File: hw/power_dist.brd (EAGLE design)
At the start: 80 x 50 mm, 78 parts, among them J1 JST-ZH6SMT_VERT, J2 JST-PH4SMT_VERT, J3 JST-PH5VERT, P1 XT30P, P2 XT30P, P3 XT30P, P4 XT30P, P5 XT30P, P6 XT30P, P7 XT90PW-M, Q1 PSMN4R8-100BSEJ, Q2 PSMN4R8-100BSEJ, Q3 PSMN4R8-100BSEJ, Q4 MF-DSC-SOT233-MMBT3904, Q5 MMBT5401 100V, U1 MAX15062AATA+T, U2 STM32G474CEU6, U4 TCAN334G, U5 LT1787HVIMS8PBF, U6 LTC4830, X3 FSV10150VTO277-3L_ONS-L

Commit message: Fine place silks
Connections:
- net GND: no longer D3.2
- net PGND: now also D3.2
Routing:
- net CAN_TX: track 29.5 -> 30.1 mm
- net GND: vias 54 -> 48
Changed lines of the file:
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@@
 <attribute name="HOUSEPART" value="1" x="62.3" y="9.9" size="1.778" layer="27" display="off"/>
 <attribute name="MPN" value="MF-CAP-0603-0.1uF" x="62.3" y="9.9" size="1.778" layer="27" display="off"/>
-<attribute name="NAME" x="63" y="9" size="0.6" layer="25" font="vector" ratio="10" rot="R180"/>
+<attribute name="NAME" x="63.8" y="9" size="0.6" layer="25" font="vector" ratio="10" rot="R180"/>
 <attribute name="POPULATE" value="1" x="62.3" y="9.9" size="1.778" layer="27" display="off"/>
 <attribute name="TOLERANCE" value="" x="62.3" y="9.9" size="1.778" layer="27" display="off"/>
@@
 <attribute name="MF" value="TDK" x="48.85" y="16.2" size="1.778" layer="27" rot="R90" display="off"/>
 <attribute name="MPN" value="C3216X7R1H106K160AE" x="48.85" y="16.2" size="1.778" layer="27" rot="R90" display="off"/>
-<attribute name="NAME" x="49.45" y="13.95" size="0.6" layer="25" font="vector" ratio="10" rot="R180"/>
+<attribute name="NAME" x="49.45" y="13.9" size="0.6" layer="25" font="vector" ratio="10" rot="R180"/>
 <attribute name="POPULATE" value="1" x="48.85" y="16.2" size="1.778" layer="27" rot="R90" display="off"/>
 <attribute name="TOLERANCE" value="" x="48.85" y="16.2" size="1.778" layer="27" rot="R90" display="off"/>
@@
 <attribute name="MF" value="MURATA" x="18.2" y="44.8" size="1.778" layer="27" display="off"/>
 <attribute name="MPN" value="GCM21BC72A105KE36L" x="18.2" y="44.8" size="1.778" layer="27" display="off"/>
-<attribute name="NAME" x="20.8" y="44.3" size="0.6" layer="25" font="vector" ratio="10"/>
+<attribute name="NAME" x="16.4" y="44.3" size="0.6" layer="25" font="vector" ratio="10" rot="R180"/>
 <attribute name="POPULATE" value="1" x="18.2" y="44.8" size="1.778" layer="27" display="off"/>
 <attribute name="TOLERANCE" value="" x="18.2" y="44.8" size="1.778" layer="27" display="off"/>
@@
 <attribute name="HOUSEPART" value="1" x="62.2" y="13.1" size="1.778" layer="27" display="off"/>
 <attribute name="MPN" value="MF-LED-0603-RED" x="62.2" y="13.1" size="1.778" layer="27" display="off"/>
-<attribute name="NAME" x="64.5" y="12.7" size="0.6" layer="25" font="vector" ratio="10" rot="R90"/>
+<attribute name="NAME" x="63.8" y="13.75" size="0.6" layer="25" font="vector" ratio="10" rot="R270"/>
 <attribute name="POPULATE" value="1" x="62.2" y="13.1" size="1.778" layer="27" display="off"/>
 <attribute name="URL" value="" x="62.2" y="13.1" size="1.778" layer="27" display="off"/>
@@
 <attribute name="HOUSEPART" value="1" x="62.3" y="7.9" size="1.778" layer="27" rot="R180" display="off"/>
 <attribute name="MPN" value="MF-RES-0603-220" x="62.3" y="7.9" size="1.778" layer="27" rot="R180" display="off"/>
-<attribute name="NAME" x="63.8" y="12.3" size="0.6" layer="25" font="vector" ratio="10" rot="R270"/>
+<attribute name="NAME" x="63.8" y="12.15" size="0.6" layer="25" font="vector" ratio="10" rot="R270"/>
 <attribute name="POPULATE" value="1" x="62.3" y="7.9" size="1.778" layer="27" rot="R180" display="off"/>
 <attribute name="TOLERANCE" value="" x="62.3" y="7.9" size="1.778" layer="27" rot="R180" display="off"/>
@@
 <attribute name="HOUSEPART" value="1" x="62.2" y="11.2" size="1.778" layer="27" display="off"/>
 <attribute name="MPN" value="MF-LED-0603-RED" x="62.2" y="11.2" size="1.778" layer="27" display="off"/>
-<attribute name="NAME" x="64.5" y="14.3" size="0.6" layer="25" font="vector" ratio="10" rot="R90"/>
+<attribute name="NAME" x="63.8" y="15.45" size="0.6" layer="25" font="vector" ratio="10" rot="R270"/>
 <attribute name="POPULATE" value="1" x="62.2" y="11.2" size="1.778" layer="27" display="off"/>
 <attribute name="URL" value="" x="62.2" y="11.2" size="1.778" layer="27" display="off"/>
@@
 <attribute name="HOUSEPART" value="1" x="51.9" y="24" size="1.778" layer="27" rot="R270" display="off"/>
 <attribute name="MPN" value="MF-CAP-0603-0.1uF" x="51.9" y="24" size="1.778" layer="27" rot="R270" display="off"/>
-<attribute name="NAME" x="52.75" y="22.5" size="0.6" layer="25" font="vector" ratio="10" rot="R180"/>
+<attribute name="NAME" x="52.75" y="22.45" size="0.6" layer="25" font="vector" ratio="10" rot="R180"/>
 <attribute name="POPULATE" value="1" x="51.9" y="24" size="1.778" layer="27" rot="R270" display="off"/>
 <attribute name="TOLERANCE" value="" x="51.9" y="24" size="1.778" layer="27" rot="R270" display="off"/>
@@
 <attribute name="HOUSEPART" value="1" x="53.7" y="35.1" size="1.778" layer="27" display="off"/>
 <attribute name="MPN" value="" x="53.7" y="35.1" size="1.778" layer="27" display="off"/>
-<attribute name="NAME" x="52.9" y="35.9" size="0.6" layer="25" font="vector" ratio="10"/>
+<attribute name="NAME" x="52.9" y="35.9" size="0.5" layer="25" font="vector" ratio="10"/>
 <attribute name="POPULATE" value="1" x="53.7" y="35.1" size="1.778" layer="27" display="off"/>
 <attribute name="TOLERANCE" value="" x="53.7" y="35.1" size="1.778" layer="27" display="off"/>
@@
 <attribute name="HOUSEPART" value="YES" x="49.4" y="21.8" size="1.778" layer="27" rot="R270" display="off"/>
 <attribute name="MPN" value="MF-DIO-SOD123-1N4148" x="49.4" y="21.8" size="1.778" layer="27" rot="R270" display="off"/>
-<attribute name="NAME" x="49" y="24.89" size="0.6" layer="25" font="vector" ratio="10"/>
+<attribute name="NAME" x="48.95" y="24.74" size="0.6" layer="25" font="vector" ratio="10"/>
 <attribute name="POPULATE" value="1" x="49.4" y="21.8" size="1.778" layer="27" rot="R270" display="off"/>
 <attribute name="URL" value="https://factory.macrofab.com/part/MF-DIO-SOD123-1N4148" x="49.4" y="21.8" size="1.778" layer="27" rot="R270" display="off"/>
@@
 <contactref element="C3" pad="P$2"/>
 <contactref element="C4" pad="P$2"/>
-<contactref element="D3" pad="2"/>
 <contactref element="C2" pad="P$2"/>
 <contactref element="J3" pad="5"/>
@@
 <wire x1="20.3" y1="10.4" x2="19.2" y2="11.5" width="0.254" layer="1"/>
 <wire x1="19.2" y1="11.5" x2="19.2" y2="11.995" width="0.254" layer="1"/>
-<via x="27.6" y="47.1" extent="1-16" drill="0.5"/>
-<via x="27.6" y="48.3" extent="1-16" drill="0.5"/>
-<via x="27.6" y="44.6" extent="1-16" drill="0.5"/>
-<via x="27.6" y="45.8" extent="1-16" drill="0.5"/>
-<polygon width="0.1524" layer="1" thermals="no">
-<vertex x="24.8" y="48.8"/>
-<vertex x="28" y="48.8"/>
-<vertex x="28" y="44"/>
-<vertex x="24.8" y="44"/>
-</polygon>
 <contactref element="C1" pad="P$2"/>
 <via x="8.8" y="9.1" extent="1-16" drill="0.3048"/>
@@
 <contactref element="R11" pad="P$1"/>
 <contactref element="R13" pad="P$1"/>
-<via x="26.45" y="48.35" extent="1-16" drill="0.5"/>
-<via x="26.5" y="44.45" extent="1-16" drill="0.5"/>
 <polygon width="0.1524" layer="2" thermals="no" rank="2">
 <vertex x="2.8" y="49.8"/>
-<vertex x="28" y="49.8"/>
-<vertex x="28" y="44.2"/>
-<vertex x="25.8" y="42"/>
+<vertex x="24.4" y="49.8"/>
+<vertex x="24.4" y="42"/>
 <vertex x="20" y="42"/>
 <vertex x="20" y="22.6"/>
@@
 <wire x1="48.58105625" y1="11.95" x2="47.20485625" y2="10.5738" width="0.1524" layer="1"/>
 <wire x1="45.7970875" y1="10.5738" x2="44.7446875" y2="9.5214" width="0.1524" layer="1"/>
-<wire x1="29.8786" y1="9.5214" x2="27.4" y2="12" width="0.1524" layer="1"/>
+<wire x1="29.8786" y1="9.5214" x2="27.8" y2="11.6" width="0.1524" layer="1"/>
 <wire x1="44.7446875" y1="9.5214" x2="29.8786" y2="9.5214" width="0.1524" layer="1"/>
-<wire x1="27.4" y1="12" x2="27.4" y2="15" width="0.1524" layer="1"/>
-<wire x1="27.4" y1="15" x2="26.595" y2="15.805" width="0.1524" layer="1"/>
+<wire x1="27.8" y1="11.6" x2="27.8" y2="14.6" width="0.1524" layer="1"/>
+<wire x1="27.8" y1="14.6" x2="26.595" y2="15.805" width="0.1524" layer="1"/>
 <wire x1="26.595" y1="15.805" x2="24.6" y2="15.805" width="0.1524" layer="1"/>
 <wire x1="47.20485625" y1="10.5738" x2="45.7970875" y2="10.5738" width="0.1524" layer="1"/>
@@
 <wire x1="50.9732875" y1="11.45" x2="50.9446875" y2="11.4786" width="0.1524" layer="1"/>
 <wire x1="50.9446875" y1="11.4786" x2="48.5407125" y2="11.4786" width="0.1524" layer="1"/>
-<wire x1="48.5407125" y1="11.4786" x2="47.3311125" y2="10.269" width="0.1524" layer="1"/>
-<wire x1="45.92334375" y1="10.269" x2="44.87094375" y2="9.2166" width="0.1524" layer="1"/>
-<wire x1="44.87094375" y1="9.2166" x2="28.7834" y2="9.2166" width="0.1524" layer="1"/>
-<wire x1="28.7834" y1="9.2166" x2="26" y2="12" width="0.1524" layer="1"/>
-<wire x1="26" y1="12" x2="24.605" y2="12" width="0.1524" layer="1"/>
+<wire x1="48.5407125" y1="11.4786" x2="46.5311125" y2="9.469" width="0.1524" layer="1"/>
+<wire x1="45.92334375" y1="9.469" x2="44.87094375" y2="8.4166" width="0.1524" layer="1"/>
+<wire x1="44.87094375" y1="8.4166" x2="29.3834" y2="8.4166" width="0.1524" layer="1"/>
+<wire x1="29.3834" y1="8.4166" x2="25.8" y2="12" width="0.1524" layer="1"/>
+<wire x1="25.8" y1="12" x2="24.605" y2="12" width="0.1524" layer="1"/>
 <wire x1="24.605" y1="12" x2="24.6" y2="11.995" width="0.1524" layer="1"/>
-<wire x1="47.3311125" y1="10.269" x2="45.92334375" y2="10.269" width="0.1524" layer="1"/>
+<wire x1="46.5311125" y1="9.469" x2="45.92334375" y2="9.469" width="0.1524" layer="1"/>
 </signal>
 <signal name="CAN_P">
@@
 </polygon>
 <contactref element="SH4" pad="2"/>
+<contactref element="D3" pad="2"/>
+<via x="26.45" y="48.35" extent="1-16" drill="0.5"/>
+<via x="27.6" y="48.35" extent="1-16" drill="0.5"/>
+<via x="27.6" y="47.15" extent="1-16" drill="0.5"/>
+<via x="27.6" y="45.8" extent="1-16" drill="0.5"/>
+<via x="27.6" y="44.6" extent="1-16" drill="0.5"/>
+<via x="26.45" y="44.5" extent="1-16" drill="0.5"/>
+<polygon width="0.1524" layer="16" thermals="no">
+<vertex x="20" y="49.2"/>
+<vertex x="29" y="49.2"/>
+<vertex x="29" y="24.2"/>
+<vertex x="20" y="24.2"/>
+</polygon>
+<polygon width="0.1524" layer="1" thermals="no">
+<vertex x="24.8" y="48.8"/>
+<vertex x="28" y="48.8"/>
+<vertex x="28" y="44"/>
+<vertex x="24.8" y="44"/>
+</polygon>
 </signal>
 <signal name="3V3_EN">

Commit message: Fix a few minor glitches
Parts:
- renumbered !6 to R16
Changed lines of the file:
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@@
 <vertex x="14.77" y="2.67"/>
 <vertex x="15.34" y="2.88"/>
-<vertex x="15.45" y="2.74"/>
-<vertex x="15.59" y="2.61"/>
-<vertex x="15.91" y="2.93"/>
+<vertex x="15.491509375" y="2.68716875"/>
+<vertex x="15.79" y="2.41"/>
+<vertex x="16.11" y="2.73"/>
 <vertex x="15.69" y="3.15"/>
 <vertex x="15.46" y="3.42"/>
@@
 <attribute name="WATTAGE" value="" x="64.6" y="48.4" size="1.778" layer="27" rot="R90" display="off"/>
 </element>
-<element name="!6" library="mfpassives" package="R0603" value="500k" x="62.6" y="48.4" smashed="yes" rot="R90">
+<element name="R16" library="mfpassives" package="R0603" value="500k" x="62.6" y="48.4" smashed="yes" rot="R90">
 <attribute name="HOUSEPART" value="1" x="62.6" y="48.4" size="1.778" layer="27" rot="R90" display="off"/>
 <attribute name="MPN" value="" x="62.6" y="48.4" size="1.778" layer="27" rot="R90" display="off"/>
-<attribute name="NAME" x="61.75" y="48.8" size="0.6" layer="25" font="vector" ratio="10" rot="R90"/>
+<attribute name="NAME" x="61.8" y="47.7" size="0.5" layer="25" font="vector" ratio="10" rot="R90"/>
 <attribute name="POPULATE" value="1" x="62.6" y="48.4" size="1.778" layer="27" rot="R90" display="off"/>
 <attribute name="TOLERANCE" value="" x="62.6" y="48.4" size="1.778" layer="27" rot="R90" display="off"/>
@@
 <signal name="PWR_SW">
 <contactref element="J2" pad="3"/>
-<contactref element="!6" pad="P$2"/>
+<contactref element="R16" pad="P$2"/>
 <contactref element="R17" pad="P$2"/>
 <wire x1="64.6" y1="49.15" x2="62.6" y2="49.15" width="0.3048" layer="1"/>
@@
 </signal>
 <signal name="N$17">
-<contactref element="!6" pad="P$1"/>
+<contactref element="R16" pad="P$1"/>
 <contactref element="D6" pad="ANODE"/>
 <wire x1="62.6" y1="47.65" x2="62.6" y2="45.875" width="0.3048" layer="1"/>
@@
 <contactref element="C15" pad="P$2"/>
 <polygon width="0.1524" layer="1" thermals="no">
-<vertex x="64.6" y="2.6"/>
-<vertex x="70" y="2.6"/>
+<vertex x="64.6" y="3.8"/>
+<vertex x="70.85714375" y="3.8"/>
 <vertex x="71" y="4"/>
 <vertex x="72.8" y="4"/>
@@
 <via x="65" y="2" extent="1-16" drill="0.5"/>
 <via x="65" y="0.8" extent="1-16" drill="0.5"/>
-<via x="66.8" y="0.8" extent="1-16" drill="0.5"/>
-<via x="68.2" y="0.8" extent="1-16" drill="0.5"/>
-<via x="69.6" y="0.8" extent="1-16" drill="0.5"/>
+<via x="65" y="3.2" extent="1-16" drill="0.5"/>
+<via x="70.8" y="1.8" extent="1-16" drill="0.5"/>
 <via x="70.8" y="0.8" extent="1-16" drill="0.5"/>
 <via x="72.2" y="0.8" extent="1-16" drill="0.5"/>
-<via x="71.6" y="2" extent="1-16" drill="0.5"/>
+<via x="72.2" y="1.8" extent="1-16" drill="0.5"/>
 <polygon width="0.1524" layer="1" thermals="no">
 <vertex x="18.8" y="30"/>

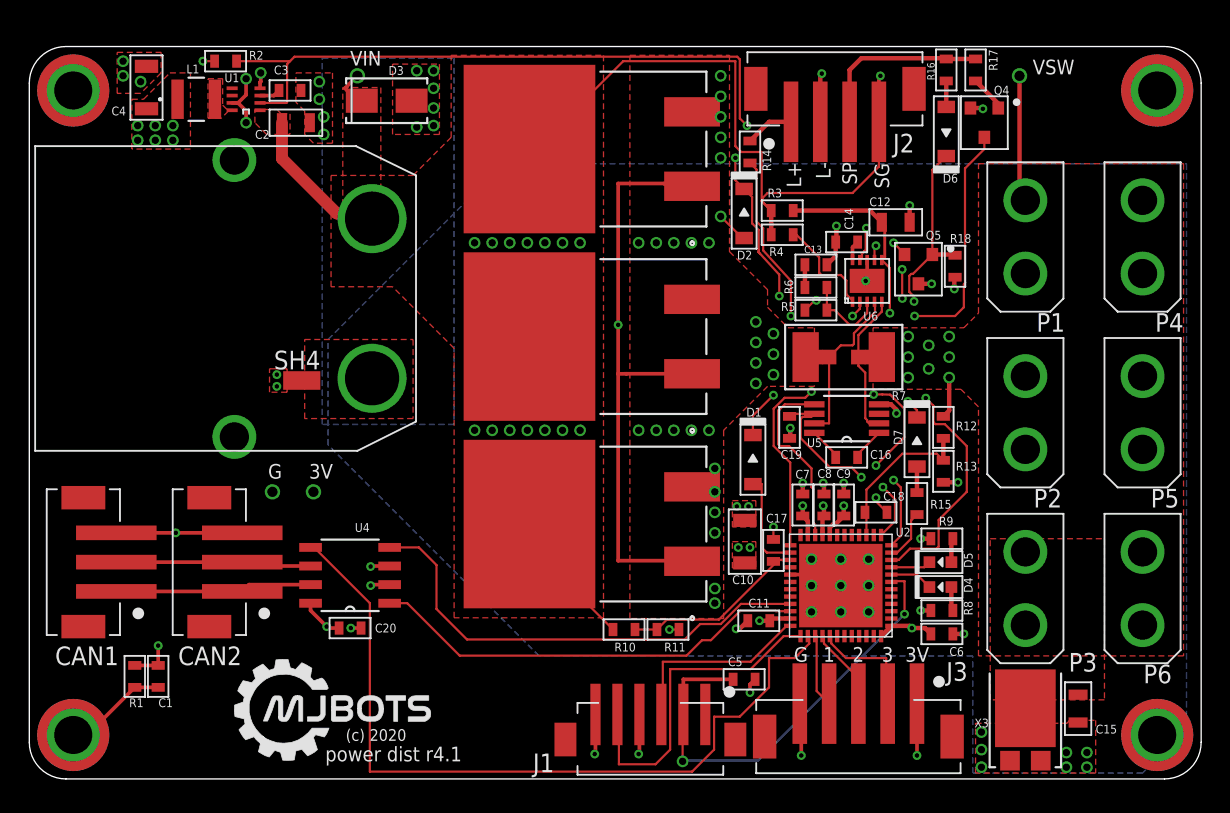
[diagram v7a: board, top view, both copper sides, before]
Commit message: Fix more minor layout and naming glitches
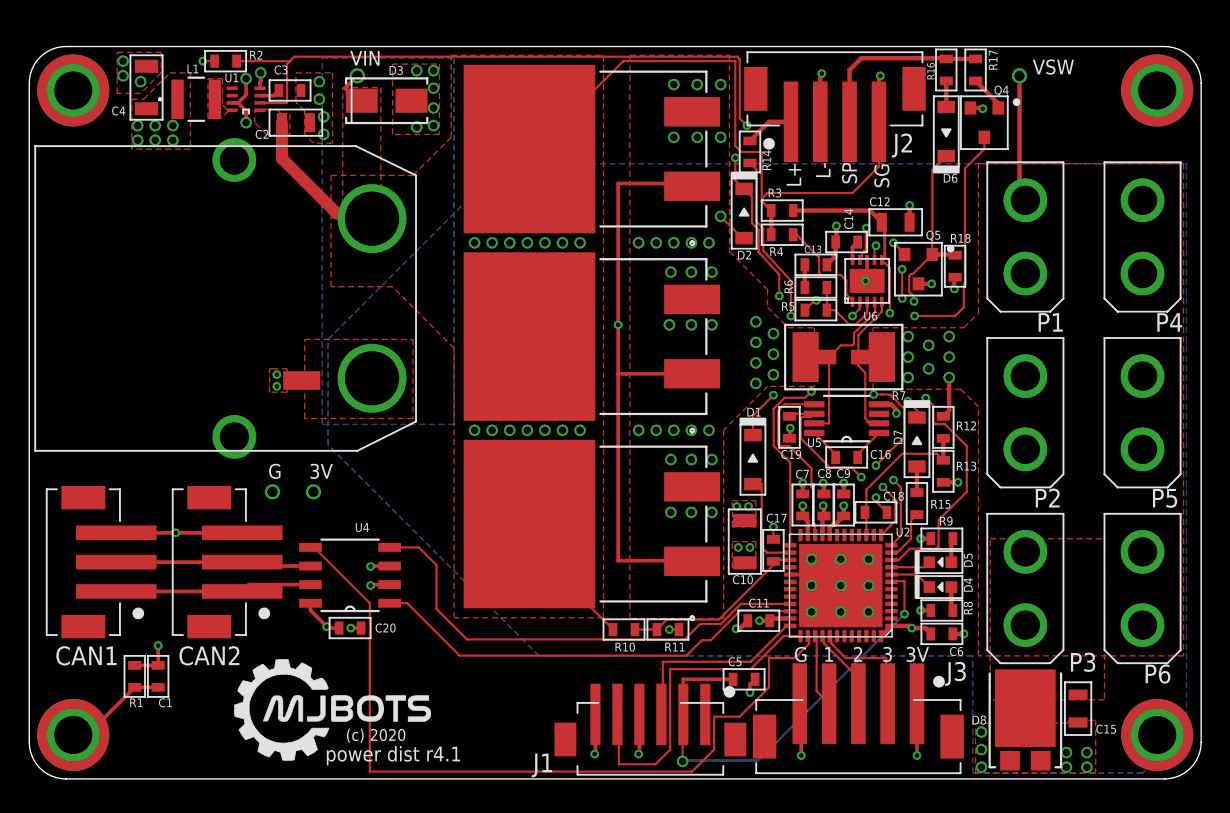
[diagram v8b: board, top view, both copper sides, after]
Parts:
- renumbered X3 to D8
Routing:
- net VIN_POST: vias 29 -> 36
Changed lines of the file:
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@@
 </polygon>
 <polygon width="0.05" layer="25">
-<vertex x="15.91" y="2.93"/>
-<vertex x="15.641825" y="1.857296875"/>
+<vertex x="15.86748125" y="2.959921875"/>
+<vertex x="15.598428125" y="1.8837125"/>
 <vertex x="15.871825" y="1.717296875"/>
 <vertex x="16.111825" y="1.587296875"/>
@@
 <attribute name="VENDOR" value="Vishay" x="24.4" y="46.3" size="1.778" layer="27" display="off"/>
 </element>
-<element name="X3" library="power_dist" package="TO277-3L_ONS-L" value="FSV10150VTO277-3L_ONS-L" x="68" y="4" smashed="yes">
+<element name="D8" library="power_dist" package="TO277-3L_ONS-L" value="FSV10150VTO277-3L_ONS-L" x="68" y="4" smashed="yes">
 <attribute name="BUILT_BY" value="EMA_Jessica" x="68" y="4" size="1.778" layer="27" display="off"/>
 <attribute name="COPYRIGHT" value="Copyright (C) 2018 Accelerated Designs. All rights reserved" x="68" y="4" size="1.778" layer="27" display="off"/>
 <attribute name="MANUFACTURER_PART_NUMBER" value="FSV10150V" x="68" y="4" size="1.778" layer="27" display="off"/>
 <attribute name="MPN" value="FSV10150V" x="68" y="4" size="1.778" layer="27" display="off"/>
-<attribute name="NAME" x="64.5234" y="3.515" size="0.6" layer="25" ratio="10" rot="SR0"/>
+<attribute name="NAME" x="64.3234" y="3.715" size="0.6" layer="25" ratio="10" rot="SR0"/>
 <attribute name="POPULATE" value="1" x="68" y="4" size="1.778" layer="27" display="off"/>
 <attribute name="SOURCELIBRARY" value="ON_Semiconductor_2019-12-30" x="68" y="4" size="1.778" layer="27" display="off"/>
@@
 </element>
 <element name="SH4" library="shorts" package="SHORT_TOP-BIG" value="SHORTBIG" x="18.6" y="27.2" smashed="yes" rot="R180">
-<attribute name="NAME" x="19.87" y="29.232" size="1.27" layer="25" ratio="16" rot="R180"/>
 <attribute name="POPULATE" value="0" x="18.6" y="26.8" size="1.778" layer="27" rot="R180" display="off"/>
 </element>
@@
 <contactref element="P2" pad="2"/>
 <contactref element="P1" pad="2"/>
-<contactref element="X3" pad="3"/>
+<contactref element="D8" pad="3"/>
 <contactref element="C15" pad="P$1"/>
 <contactref element="DB_VSW" pad="P$1"/>
@@
 <via x="49.6" y="28.4" extent="1-16" drill="0.5"/>
 <via x="49.6" y="27" extent="1-16" drill="0.5"/>
-<via x="46.8" y="12" extent="1-16" drill="0.5"/>
-<via x="46.8" y="13" extent="1-16" drill="0.5"/>
-<via x="46.8" y="16.8" extent="1-16" drill="0.5"/>
-<via x="46.8" y="18.2" extent="1-16" drill="0.5"/>
-<via x="46.8" y="19.6" extent="1-16" drill="0.5"/>
-<via x="46.8" y="21.2" extent="1-16" drill="0.5"/>
-<via x="47.2" y="48" extent="1-16" drill="0.5"/>
-<via x="47.2" y="46.6" extent="1-16" drill="0.5"/>
-<via x="47.2" y="45.2" extent="1-16" drill="0.5"/>
-<via x="47.2" y="43.8" extent="1-16" drill="0.5"/>
-<via x="47.2" y="42.4" extent="1-16" drill="0.5"/>
+<via x="46.6" y="18.2" extent="1-16" drill="0.5"/>
+<via x="45.2" y="18.2" extent="1-16" drill="0.5"/>
+<via x="43.8" y="18.2" extent="1-16" drill="0.5"/>
+<via x="46.6" y="21.8" extent="1-16" drill="0.5"/>
+<via x="45.2" y="21.8" extent="1-16" drill="0.5"/>
+<via x="43.8" y="21.8" extent="1-16" drill="0.5"/>
+<via x="44" y="47.4" extent="1-16" drill="0.5"/>
+<via x="45.6" y="47.4" extent="1-16" drill="0.5"/>
+<via x="44" y="43.8" extent="1-16" drill="0.5"/>
+<via x="45.6" y="43.8" extent="1-16" drill="0.5"/>
+<via x="47.2" y="47.4" extent="1-16" drill="0.5"/>
 <via x="47.2" y="38.4" extent="1-16" drill="0.5"/>
 <contactref element="D2" pad="ANODE"/>
 <wire x1="48.8" y1="36.925" x2="48.675" y2="36.925" width="0.1524" layer="1"/>
 <wire x1="48.675" y1="36.925" x2="47.2" y2="38.4" width="0.1524" layer="1"/>
+<via x="47.2" y="43.8" extent="1-16" drill="0.5"/>
+<via x="43.8" y="34.6" extent="1-16" drill="0.5"/>
+<via x="45.2" y="34.6" extent="1-16" drill="0.5"/>
+<via x="46.6" y="34.6" extent="1-16" drill="0.5"/>
+<via x="43.7" y="31" extent="1-16" drill="0.5"/>
+<via x="45.2" y="31" extent="1-16" drill="0.5"/>
+<via x="46.6" y="31" extent="1-16" drill="0.5"/>
 </signal>
 <signal name="N$5">
@@
 <vertex x="34.8" y="8.4"/>
 </polygon>
-<contactref element="X3" pad="1"/>
-<contactref element="X3" pad="2"/>
-<contactref element="C15" pad="P$2"/>
 <polygon width="0.1524" layer="1" thermals="no">
 <vertex x="64.6" y="3.8"/>
@@
 <vertex x="24.8" y="44"/>
 </polygon>
+<contactref element="D8" pad="1"/>
+<contactref element="D8" pad="2"/>
+<contactref element="C15" pad="P$2"/>
 </signal>
 <signal name="3V3_EN">
